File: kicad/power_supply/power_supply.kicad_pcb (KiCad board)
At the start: 2 copper layers, 4 parts

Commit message: Commit
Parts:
- added C1: 1u, Capacitor_SMD:C_0805_2012Metric_Pad1.18x1.45mm_HandSolder, F.Cu at (35.4, 41.0)
- added C14: 47u, Capacitor_SMD:C_0805_2012Metric_Pad1.18x1.45mm_HandSolder, F.Cu at (40.2, 47.0)
- added C15: 47u, Capacitor_SMD:C_0805_2012Metric_Pad1.18x1.45mm_HandSolder, F.Cu at (40.2, 50.0)
- added C16: 47u, Capacitor_SMD:C_0805_2012Metric_Pad1.18x1.45mm_HandSolder, F.Cu at (45.0, 41.0)
- added C17: 47u, Capacitor_SMD:C_0805_2012Metric_Pad1.18x1.45mm_HandSolder, F.Cu at (45.0, 44.0)
- added C18: 100n, Capacitor_SMD:C_0805_2012Metric_Pad1.18x1.45mm_HandSolder, F.Cu at (45.0, 47.0)
- added C19: 1u, Capacitor_SMD:C_0805_2012Metric_Pad1.18x1.45mm_HandSolder, F.Cu at (45.0, 50.0)
- added C7: 100n, Capacitor_SMD:C_0805_2012Metric_Pad1.18x1.45mm_HandSolder, F.Cu at (35.4, 50.0)
- added C8: 47u, Capacitor_SMD:C_0805_2012Metric_Pad1.18x1.45mm_HandSolder, F.Cu at (40.2, 41.0)
- added C9: 47u, Capacitor_SMD:C_0805_2012Metric_Pad1.18x1.45mm_HandSolder, F.Cu at (40.2, 44.0)
- added J2: USB_C_Receptacle_USB2.0, Connector_USB:USB_C_Receptacle_GCT_USB4085, F.Cu at (6.03, 57.0)
- added J6: Conn_02x08_Odd_Even, Connector_PinSocket_2.54mm:PinSocket_2x08_P2.54mm_Vertical, F.Cu at (60.0, 76.4)
- added JP1: Jumper_2_Open, Jumper:SolderJumper-2_P1.3mm_Open_Pad1.0x1.5mm, F.Cu at (2.35, 53.0)
- added Q7: NPN, Package_TO_SOT_THT:TO-220-3_Vertical, F.Cu at (50.6, 43.4)
- added Q8: PNP, Package_TO_SOT_THT:TO-220-3_Vertical, F.Cu at (50.6, 49.4)
- added R10: 22k, Resistor_SMD:R_0805_2012Metric_Pad1.20x1.40mm_HandSolder, F.Cu at (40.1, 38.0)
- added R11: 10k, Resistor_SMD:R_0805_2012Metric_Pad1.20x1.40mm_HandSolder, F.Cu at (44.8, 26.2)
- added R12: 10k, Resistor_SMD:R_0805_2012Metric_Pad1.20x1.40mm_HandSolder, F.Cu at (44.8, 29.2)
- added R15: 3k3, Resistor_SMD:R_0805_2012Metric_Pad1.20x1.40mm_HandSolder, F.Cu at (44.8, 32.1)
- added R16: 3k3, Resistor_SMD:R_0805_2012Metric_Pad1.20x1.40mm_HandSolder, F.Cu at (44.8, 35.1)
- added R17: 33k, Resistor_SMD:R_0805_2012Metric_Pad1.20x1.40mm_HandSolder, F.Cu at (44.8, 38.0)
- added R18: 1k, Resistor_SMD:R_0805_2012Metric_Pad1.20x1.40mm_HandSolder, F.Cu at (49.6, 26.2)
- added R19: 1k, Resistor_SMD:R_0805_2012Metric_Pad1.20x1.40mm_HandSolder, F.Cu at (49.6, 29.2)
- added R20: 33k, Resistor_SMD:R_0805_2012Metric_Pad1.20x1.40mm_HandSolder, F.Cu at (49.6, 32.1)
- added R23: 10k, Resistor_SMD:R_0805_2012Metric_Pad1.20x1.40mm_HandSolder, F.Cu at (49.6, 35.1)
- added R24: 16k, Resistor_SMD:R_0805_2012Metric_Pad1.20x1.40mm_HandSolder, F.Cu at (49.6, 38.0)
- added R3: 22, Resistor_SMD:R_0805_2012Metric_Pad1.20x1.40mm_HandSolder, F.Cu at (35.3, 32.1)
- added R4: 22, Resistor_SMD:R_0805_2012Metric_Pad1.20x1.40mm_HandSolder, F.Cu at (35.3, 35.1)
- added R5: 1k5, Resistor_SMD:R_0805_2012Metric_Pad1.20x1.40mm_HandSolder, F.Cu at (35.3, 38.0)
- added R6: 1M, Resistor_SMD:R_0805_2012Metric_Pad1.20x1.40mm_HandSolder, F.Cu at (40.1, 26.2)
- added R7: 22k, Resistor_SMD:R_0805_2012Metric_Pad1.20x1.40mm_HandSolder, F.Cu at (40.1, 29.2)
- added R8: 10k, Resistor_SMD:R_0805_2012Metric_Pad1.20x1.40mm_HandSolder, F.Cu at (40.1, 32.1)
- added R9: 10k, Resistor_SMD:R_0805_2012Metric_Pad1.20x1.40mm_HandSolder, F.Cu at (40.1, 35.1)
- added TH2: 20R->1R, Capacitor_THT:C_Disc_D9.0mm_W5.0mm_P5.00mm, F.Cu at (54.7, 28.0)
- added TH3: 20R->1R, Capacitor_THT:C_Disc_D9.0mm_W5.0mm_P5.00mm, F.Cu at (54.7, 34.6)
- added U1: PCM2707CPJTR, Package_QFP:TQFP-32_7x7mm_P0.8mm, F.Cu at (10.0, 72.0)
- added U2: LM317, Package_TO_SOT_SMD:SOT-89-3, F.Cu at (29.2, 50.2)
- C5: value 10u -> 100n
- R1: value 10k -> 5.1k
- R2: value 10k -> 1k5
- moved C5 23.7 mm to (35.4, 44.0)
- moved C6 23.5 mm to (35.4, 47.0)
- moved R1 16.6 mm to (35.3, 26.2)
- moved R2 16.1 mm to (35.3, 29.2)
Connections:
- C5 pad 1: +36V -> GNDD
- C5 pad 2: GND -> +3V3
- C6 pad 1: GND -> GNDD
- C6 pad 2: -36V -> Net-(U1-VCOM)
- R1 pad 1: +36V -> Net-(J2-CC1)
- R1 pad 2: GND -> GNDD
- R2 pad 1: GND -> Net-(D3-A2)
- R2 pad 2: -36V -> +3V3
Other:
- board outline added: 62 x 99 mm

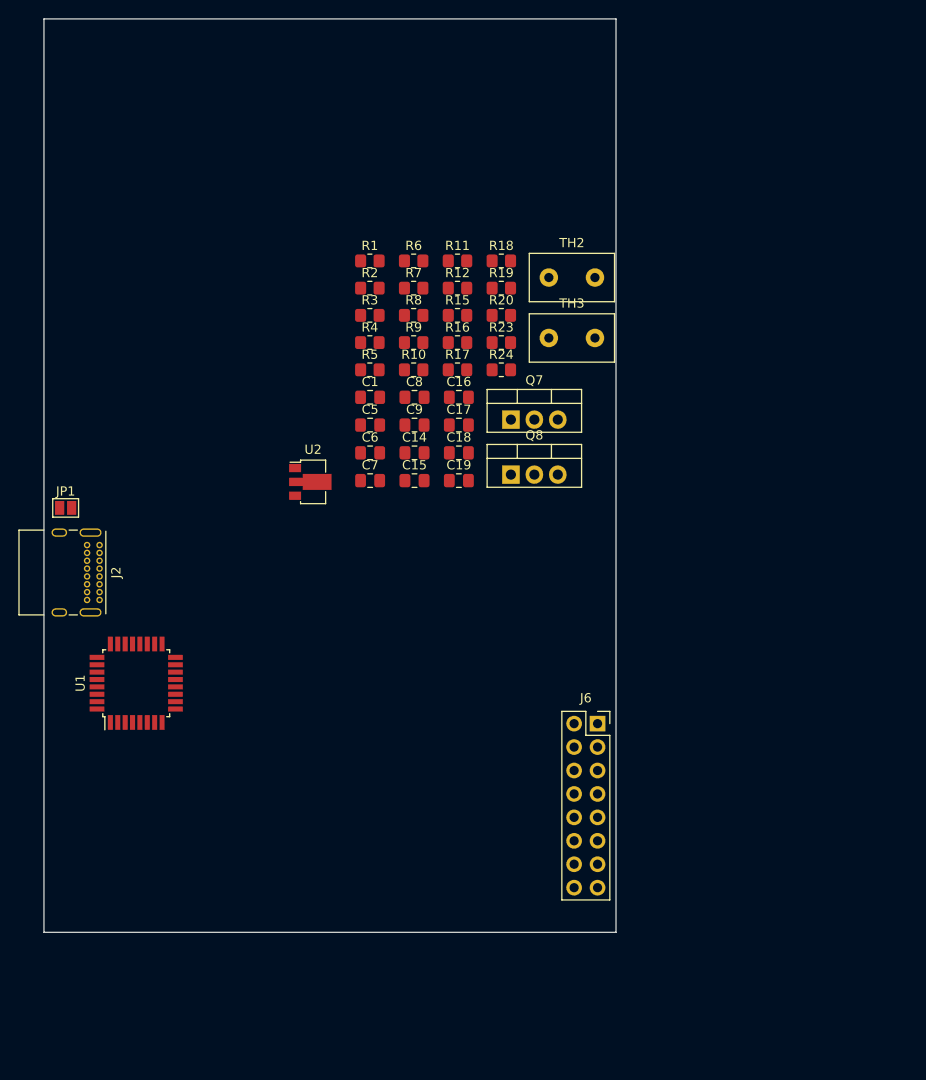
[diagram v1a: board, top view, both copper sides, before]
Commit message: completed power supply footprints and placement
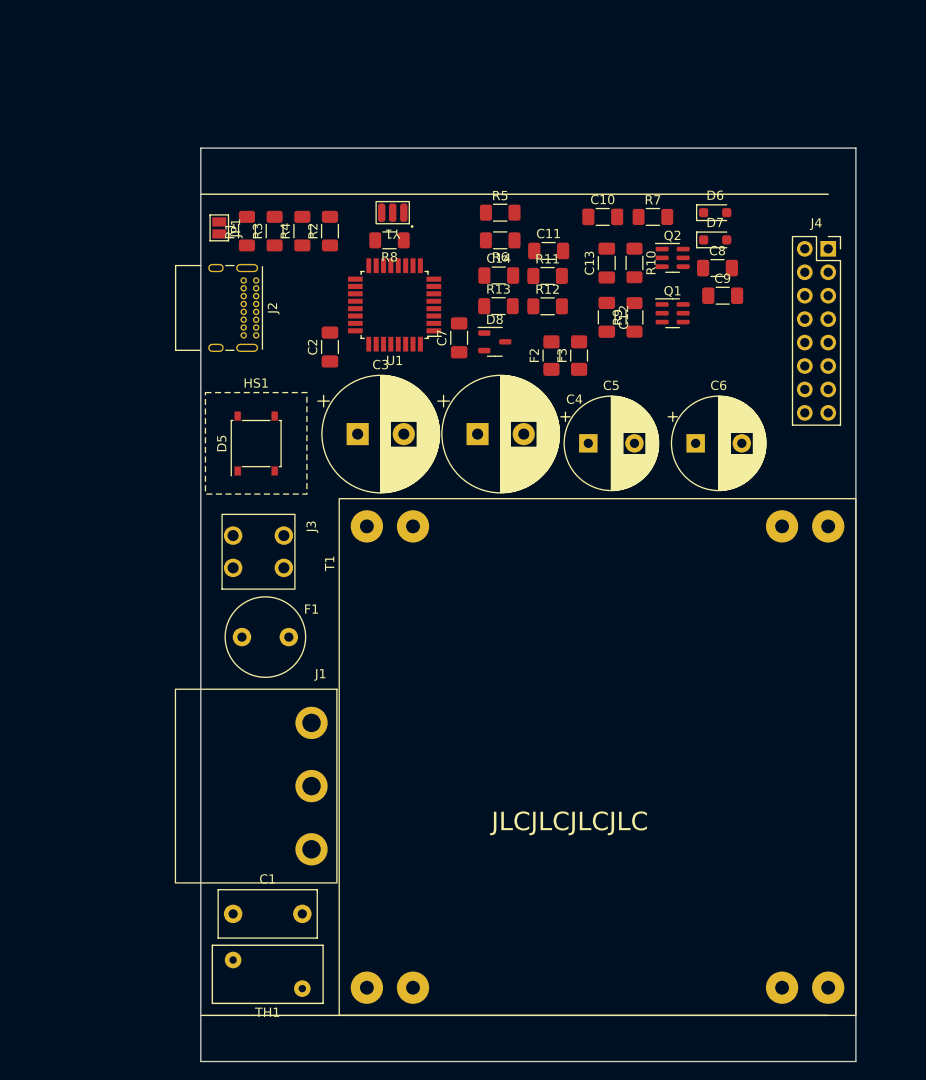
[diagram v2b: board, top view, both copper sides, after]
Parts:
- removed C15, C16, C17: 47u, Capacitor_SMD:C_0805_2012Metric_Pad1.18x1.45mm_HandSolder
- removed C18: 100n, Capacitor_SMD:C_0805_2012Metric_Pad1.18x1.45mm_HandSolder
- removed C19: 1u, Capacitor_SMD:C_0805_2012Metric_Pad1.18x1.45mm_HandSolder
- removed J6: Conn_02x08_Odd_Even, Connector_PinSocket_2.54mm:PinSocket_2x08_P2.54mm_Vertical
- removed Q7: NPN, Package_TO_SOT_THT:TO-220-3_Vertical
- removed Q8: PNP, Package_TO_SOT_THT:TO-220-3_Vertical
- removed R15, R16: 3k3, Resistor_SMD:R_0805_2012Metric_Pad1.20x1.40mm_HandSolder
- removed R17, R20: 33k, Resistor_SMD:R_0805_2012Metric_Pad1.20x1.40mm_HandSolder
- removed R18, R19: 1k, Resistor_SMD:R_0805_2012Metric_Pad1.20x1.40mm_HandSolder
- removed R23: 10k, Resistor_SMD:R_0805_2012Metric_Pad1.20x1.40mm_HandSolder
- removed R24: 16k, Resistor_SMD:R_0805_2012Metric_Pad1.20x1.40mm_HandSolder
- removed TH2, TH3: 20R->1R, Capacitor_THT:C_Disc_D9.0mm_W5.0mm_P5.00mm
- removed U2: LM317, Package_TO_SOT_SMD:SOT-89-3
- added C10: 10u, Capacitor_SMD:C_1206_3216Metric_Pad1.33x1.80mm_HandSolder, F.Cu at (60.6, 21.5)
- added C11: 100n, Capacitor_SMD:C_1206_3216Metric_Pad1.33x1.80mm_HandSolder, F.Cu at (54.7, 25.1)
- added C12: 10u, Capacitor_SMD:C_1206_3216Metric_Pad1.33x1.80mm_HandSolder, F.Cu at (61.0, 32.3)
- added C13: 10u, Capacitor_SMD:C_1206_3216Metric_Pad1.33x1.80mm_HandSolder, F.Cu at (61.0, 26.5)
- added C2: 1u, Capacitor_SMD:C_1206_3216Metric_Pad1.33x1.80mm_HandSolder, F.Cu at (31.0, 35.6)
- added C3: 2m2, Capacitor_THT:CP_Radial_D12.5mm_P5.00mm, F.Cu at (34.0, 45.0)
- added C4: 2m2, Capacitor_THT:CP_Radial_D12.5mm_P5.00mm, F.Cu at (47.0, 45.0)
- added D5: ~, Diode_SMD:Diode_Bridge_Vishay_MBLS, F.Cu at (23.0, 46.0)
- added D6: D, Diode_SMD:D_SOD-323_HandSoldering, F.Cu at (72.8, 21.0)
- added D7: D, Diode_SMD:D_SOD-323_HandSoldering, F.Cu at (72.8, 23.9)
- added D8: ~, Package_TO_SOT_SMD:SOT-23-3, F.Cu at (48.9, 35.0)
- added F1: 80mA, Fuse:Fuse_Littelfuse_372_D8.50mm, F.Cu at (26.5, 67.0)
- added F2: 1A, Fuse:Fuse_1206_3216Metric_Pad1.42x1.75mm_HandSolder, F.Cu at (55.0, 36.5)
- added F3: 1A, Fuse:Fuse_1206_3216Metric_Pad1.42x1.75mm_HandSolder, F.Cu at (58.0, 36.5)
- added HS1: Heatsink, library:Heatsink_10x10, F.Cu at (23.0, 46.0)
- added J1: Conn_WallSocket_Earth, library:WallSocket_Schurter_6160.0003, F.Cu at (29.0, 83.2)
- added J3: Conn_01x02, library:WAGO_2086-11X2, F.Cu at (23.2, 57.8)
- added J4: Conn_02x08_Odd_Even, Connector_PinSocket_2.54mm:PinSocket_2x08_P2.54mm_Vertical, F.Cu at (85.0, 24.9)
- added Q1: BCM53DS, Package_SO:SC-74-6_1.5x2.9mm_P0.95mm, F.Cu at (68.1, 31.9)
- added Q2: BCM56DS, Package_SO:SC-74-6_1.5x2.9mm_P0.95mm, F.Cu at (68.1, 25.9)
- added R13: 16, Resistor_SMD:R_1206_3216Metric_Pad1.30x1.75mm_HandSolder, F.Cu at (49.3, 31.1)
- added T1: 70043K, library:Talema_Transformer_2P2S_10VA, F.Cu at (60.0, 80.0)
- added TH1: MOV, Varistor:RV_Disc_D12mm_W6.3mm_P7.5mm, F.Cu at (20.5, 102.0)
- added Y1: 12MHz±0.05%, library:Resonator_Murata, F.Cu at (37.8, 21.0)
- C1: value 1u -> 3n9; footprint Capacitor_SMD:C_0805_2012Metric_Pad1.18x1.45mm_HandSolder -> Capacitor_THT:C_Disc_D10.5mm_W5.0mm_P7.50mm
- C14, C9: value 47u -> 100n; footprint Capacitor_SMD:C_0805_2012Metric_Pad1.18x1.45mm_HandSolder -> Capacitor_SMD:C_1206_3216Metric_Pad1.33x1.80mm_HandSolder
- C5: value 100n -> 470u; footprint Capacitor_SMD:C_0805_2012Metric_Pad1.18x1.45mm_HandSolder -> Capacitor_THT:CP_Radial_D10.0mm_P5.00mm
- C6: value 10u -> 470u; footprint Capacitor_SMD:C_0805_2012Metric_Pad1.18x1.45mm_HandSolder -> Capacitor_THT:CP_Radial_D10.0mm_P5.00mm
- C7: value 100n -> 10u; footprint Capacitor_SMD:C_0805_2012Metric_Pad1.18x1.45mm_HandSolder -> Capacitor_SMD:C_1206_3216Metric_Pad1.33x1.80mm_HandSolder
- C8: value 47u -> 10u; footprint Capacitor_SMD:C_0805_2012Metric_Pad1.18x1.45mm_HandSolder -> Capacitor_SMD:C_1206_3216Metric_Pad1.33x1.80mm_HandSolder
- R1, R11, R12, R2, R3, R4, R9: footprint Resistor_SMD:R_0805_2012Metric_Pad1.20x1.40mm_HandSolder -> Resistor_SMD:R_1206_3216Metric_Pad1.30x1.75mm_HandSolder
- R10: value 22k -> 10k; footprint Resistor_SMD:R_0805_2012Metric_Pad1.20x1.40mm_HandSolder -> Resistor_SMD:R_1206_3216Metric_Pad1.30x1.75mm_HandSolder
- R5: value 1k5 -> 10k; footprint Resistor_SMD:R_0805_2012Metric_Pad1.20x1.40mm_HandSolder -> Resistor_SMD:R_1206_3216Metric_Pad1.30x1.75mm_HandSolder
- R6: value 1M -> 10k; footprint Resistor_SMD:R_0805_2012Metric_Pad1.20x1.40mm_HandSolder -> Resistor_SMD:R_1206_3216Metric_Pad1.30x1.75mm_HandSolder
- R7: value 22k -> 1k5; footprint Resistor_SMD:R_0805_2012Metric_Pad1.20x1.40mm_HandSolder -> Resistor_SMD:R_1206_3216Metric_Pad1.30x1.75mm_HandSolder
- R8: value 10k -> 1M; footprint Resistor_SMD:R_0805_2012Metric_Pad1.20x1.40mm_HandSolder -> Resistor_SMD:R_1206_3216Metric_Pad1.30x1.75mm_HandSolder
- U1: value PCM2707CPJTR -> PCM2706CPJTR
- moved C1 57.9 mm to (20.5, 97.0)
- moved U1 49.6 mm to (38.0, 31.0), turned to 180 degrees
- moved C9 36.2 mm to (73.6, 30.0)
- moved C8 35.7 mm to (73.0, 27.0)
- moved C6 35.3 mm to (70.6, 46.0)
- moved JP1 34.6 mm to (19.0, 22.6), turned to -90 degrees
- moved J2 33.3 mm to (23.0, 28.4)
- moved R7 27.1 mm to (66.0, 21.5)
- moved R10 26.6 mm to (64.0, 26.4), turned to -90 degrees
- moved R9 24.1 mm to (64.0, 32.4), turned to 90 degrees
- moved C5 23.7 mm to (59.0, 46.0)
- moved R5 22.1 mm to (49.5, 21.0)
- moved C14 21.3 mm to (49.3, 27.8)
- moved C7 18.2 mm to (45.0, 34.6), turned to 90 degrees
- moved R4 14.1 mm to (28.0, 23.0), turned to 90 degrees
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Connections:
- net Net-(D2-A2) renamed /CONN_D-
- net Net-(D3-A2) renamed /CONN_D+
- net Net-(U1-D+) renamed /D+
- net Net-(U1-D-) renamed /D-
- C1 pad 1: GNDD -> Net-(J3-Pin_1)
- C1 pad 2: VBUS -> /NEUTRAL
- C14 pad 1: +30V -> GND
- C14 pad 2: GND -> Net-(D8-A)
- C5 pad 1: GNDD -> +25V
- C5 pad 2: +3V3 -> GND
- C6 pad 1: GNDD -> GND
- C6 pad 2: Net-(U1-VCOM) -> -25V
- C7 pad 1: GNDD -> Net-(C7-Pad1)
- C7 pad 2: Net-(U1-VCCP) -> GND
- C8 pad 1: Net-(Q1-G) -> GND
- C8 pad 2: GND -> Net-(C8-Pad2)
- C9 pad 1: GND -> GNDD
- C9 pad 2: Net-(Q2-G) -> +3V3
- R10 pad 1: Net-(Q2-G) -> Net-(C8-Pad2)
- R10 pad 2: Net-(D5--) -> -25V
- R11 pad 1: +30V -> Net-(C7-Pad1)
- R11 pad 2: GND -> /CM+
- R12 pad 1: GND -> Net-(C8-Pad2)
- R12 pad 2: -30V -> /CM-
- R5 pad 1: Net-(U1-DT) -> +25V
- R5 pad 2: +3V3 -> GND
- R6 pad 1: Net-(U1-XTI) -> GND
- R6 pad 2: Net-(U1-XTO) -> -25V
- R7 pad 1: Net-(D5-+) -> /DT
- R7 pad 2: Net-(Q1-G) -> +3V3
- R8 pad 1: Net-(Q1-G) -> /XTI
- R8 pad 2: GND -> /XTO
- R9 pad 1: GND -> +25V
- R9 pad 2: Net-(Q2-G) -> Net-(C7-Pad1)
- U1 pad 12: Net-(U1-XTI) -> /XTI
- U1 pad 13: Net-(U1-XTO) -> /XTO
- U1 pad 15: Net-(U1-DT) -> /DT
- U1 pad 16: GNDD -> +3V3
- U1 pad 3: VBUS -> GNDD
- U1 pad 32: Net-(U1-VCOM) -> /VCOM
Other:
- board size 62 x 99 mm -> 71 x 99 mm
- board text added: "1mm to panel PCB"
- board text added: "JLCJLCJLCJLC"

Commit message: commit
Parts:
- removed D6, D7: D, Diode_SMD:D_SOD-323_HandSoldering
- removed D8: ~, Package_TO_SOT_SMD:SOT-23-3
- removed J2: USB_C_Receptacle_USB2.0, Connector_USB:USB_C_Receptacle_GCT_USB4085
- removed Q1: BCM53DS, Package_SO:SC-74-6_1.5x2.9mm_P0.95mm
- removed Q2: BCM56DS, Package_SO:SC-74-6_1.5x2.9mm_P0.95mm
- added C15: 10u, Capacitor_SMD:C_1206_3216Metric_Pad1.33x1.80mm_HandSolder, F.Cu at (65.6, 25.8)
- added C16: 10u, Capacitor_SMD:C_1206_3216Metric_Pad1.33x1.80mm_HandSolder, F.Cu at (65.6, 29.1)
- added D1: ~, Package_TO_SOT_SMD:SOT-23-3, F.Cu at (26.9, 23.1)
- added D2: D_TVS_Quadruple, Package_TO_SOT_SMD:SOT-353_SC-70-5_Handsoldering, F.Cu at (65.3, 33.6)
- added D3: ~, Diode_SMD:Diode_Bridge_Vishay_MBLS, F.Cu at (24.0, 52.0)
- added D4: ~, Package_TO_SOT_SMD:SOT-23-3, F.Cu at (26.9, 27.6)
- added J5: Conn_02x08_Odd_Even, Connector_PinSocket_2.54mm:PinSocket_2x08_P2.54mm_Vertical, F.Cu at (91.0, 23.8)
- added R14: 1k1, Resistor_SMD:R_1206_3216Metric_Pad1.30x1.75mm_HandSolder, F.Cu at (83.5, 32.3)
- added R15: 100, Resistor_SMD:R_1206_3216Metric_Pad1.30x1.75mm_HandSolder, F.Cu at (83.5, 35.6)
- added U2: LM337_SOT223, Package_TO_SOT_SMD:SOT-223-3_TabPin2, F.Cu at (65.0, 41.0)
- added U3: PCM2706CPJTR, Package_QFP:TQFP-32_7x7mm_P0.8mm, F.Cu at (45.0, 26.0)
- C1: value 3n9 -> 100n; footprint Capacitor_THT:C_Disc_D10.5mm_W5.0mm_P7.50mm -> Capacitor_SMD:C_1206_3216Metric_Pad1.33x1.80mm_HandSolder
- C10, C13, C8: value 10u -> 100n
- C11, C9: value 100n -> 10u
- C2: value 1u -> 4n7
- C3: value 2m2 -> 3n9; footprint Capacitor_THT:CP_Radial_D12.5mm_P5.00mm -> Capacitor_THT:C_Disc_D10.5mm_W5.0mm_P7.50mm
- C4: value 2m2 -> 100n; footprint Capacitor_THT:CP_Radial_D12.5mm_P5.00mm -> Capacitor_SMD:C_1206_3216Metric_Pad1.33x1.80mm_HandSolder
- C5: value 470u -> 3u3; footprint Capacitor_THT:CP_Radial_D10.0mm_P5.00mm -> Capacitor_SMD:C_1206_3216Metric_Pad1.33x1.80mm_HandSolder
- C7: value 10u -> 470u; footprint Capacitor_SMD:C_1206_3216Metric_Pad1.33x1.80mm_HandSolder -> Capacitor_THT:CP_Radial_D10.0mm_P5.00mm
- D5: footprint Diode_SMD:Diode_Bridge_Vishay_MBLS -> Package_TO_SOT_SMD:SOT-23-3
- F2, F3: value 1A -> 500mA; footprint Fuse:Fuse_1206_3216Metric_Pad1.42x1.75mm_HandSolder -> Fuse:Fuse_Schurter_UMT250; moved to B.Cu
- J3: value Conn_01x02 -> USB_C_Receptacle_USB2.0; footprint library:WAGO_2086-11X2 -> Connector_USB:USB_C_Receptacle_GCT_USB4085
- J4: value Conn_02x08_Odd_Even -> Conn_01x02; footprint Connector_PinSocket_2.54mm:PinSocket_2x08_P2.54mm_Vertical -> library:WAGO_2086-11X2
- R1: value 5.1k -> 22
- R11: value 10k -> 1M
- R12: value 10k -> 100
- R13: value 16 -> 1k1
- R2: value 1k5 -> 33k
- R3, R4: value 22 -> 5k1
- R5: value 10k -> 1k5
- R6: value 10k -> 22
- R7: value 1k5 -> 22
- R8: value 1M -> 1k5
- T1: value 70043K -> 70063K; footprint library:Talema_Transformer_2P2S_10VA -> library:Talema_Transformer_2P2S_25VA
- U1: value PCM2706CPJTR -> LM317_SOT-223; footprint Package_QFP:TQFP-32_7x7mm_P0.8mm -> Package_TO_SOT_SMD:SOT-223-3_TabPin2
- moved C1 81.6 mm to (53.6, 22.4)
- moved J4 64.5 mm to (22.8, 41.8), turned to 90 degrees
- moved C3 53.5 mm to (21.2, 97.0)
- moved R1 49.6 mm to (71.6, 22.4), turned to 0 degrees
- moved R3 47.0 mm to (71.6, 29.0), turned to 0 degrees
- moved R4 44.6 mm to (71.6, 32.3), turned to 0 degrees
- moved R2 40.7 mm to (71.6, 25.7), turned to 0 degrees
- moved R8 40.4 mm to (77.5, 29.0), turned to 0 degrees
- moved C6 39.3 mm to (32.0, 39.0)
- moved R13 34.3 mm to (83.5, 29.0)
- moved J3 29.6 mm to (22.6, 28.2), turned to -90 degrees
- moved R11 29.4 mm to (83.5, 22.4)
- moved R12 29.4 mm to (83.5, 25.7)
- moved R6 28.1 mm to (77.5, 22.4), turned to 0 degrees
- moved R5 26.5 mm to (71.6, 35.6)
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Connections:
- C1 pad 1: Net-(J3-Pin_1) -> GND
- C1 pad 2: /NEUTRAL -> Net-(J1-EARTH)
- C10 pad 2: /VCOM -> Net-(U3-VCCP)
- C11 pad 1: GNDD -> Net-(D4-A)
- C11 pad 2: Net-(U1-VCCP) -> GND
- C12 pad 1: /CM+ -> GND
- C12 pad 2: GND -> Net-(D5-K)
- C13 pad 1: GND -> +20Vreg
- C13 pad 2: /CM- -> GND
- C14 pad 2: Net-(D8-A) -> -20Vreg
- C2 pad 1: GNDD -> Net-(D2-C)
- C2 pad 2: VBUS -> GNDD
- C3 pad 1: +25V -> Net-(J4-Pin_1)
- C3 pad 2: GND -> /NEUTRAL
- C4 pad 1: GND -> GNDD
- C4 pad 2: -25V -> VBUS
- C5 pad 1: +25V -> GNDD
- C5 pad 2: GND -> VBUS
- C6 pad 1: GND -> +25V
- C6 pad 2: -25V -> GND
- C7 pad 1: Net-(C7-Pad1) -> GND
- C7 pad 2: GND -> -25V
- C8 pad 1: GND -> GNDD
- C8 pad 2: Net-(C8-Pad2) -> +3V3
- C9 pad 2: +3V3 -> /VCOM
- D5 pad 1: /V_{rect}+ -> -25V
- D5 pad 2: /V_{tran}- -> -20Vreg
- D5 pad 3: /V_{rect}- -> Net-(D5-K)
- F1 pad 2: Net-(J3-Pin_1) -> Net-(J4-Pin_1)
- J1 pad 3: Net-(D8-A) -> Net-(J1-EARTH)
- J4 pad 1: +20Vreg -> Net-(J4-Pin_1)
- J4 pad 2: +25V -> /LIVE
- JP1 pad 2: Net-(J2-SHIELD) -> Net-(D2-C)
- R1 pad 1: Net-(J2-CC1) -> Net-(J1-EARTH)
- R1 pad 2: GNDD -> GND
- R10 pad 1: Net-(C8-Pad2) -> GND
- R11 pad 1: Net-(C7-Pad1) -> /XTI
- R11 pad 2: /CM+ -> /XTO
- R12 pad 1: Net-(C8-Pad2) -> +20Vreg
- R12 pad 2: /CM- -> Net-(D4-A)
- R13 pad 1: Net-(D8-A) -> Net-(D4-A)
- R2 pad 1: /CONN_D+ -> GNDD
- R2 pad 2: +3V3 -> Net-(D2-C)
- R3 pad 1: /CONN_D- -> Net-(J3-CC1)
- R3 pad 2: /D- -> GNDD
- R4 pad 1: /CONN_D+ -> Net-(J3-CC2)
- R4 pad 2: /D+ -> GNDD
- R5 pad 1: +25V -> /CONN_D+
- R5 pad 2: GND -> +3V3
- R6 pad 1: GND -> /CONN_D-
- R6 pad 2: -25V -> /D-
- R7 pad 1: /DT -> /CONN_D+
- R7 pad 2: +3V3 -> /D+
- R8 pad 1: /XTI -> /DT
- R8 pad 2: /XTO -> +3V3
- R9 pad 2: Net-(C7-Pad1) -> GND
- TH1 pad 1: Net-(J3-Pin_1) -> Net-(J4-Pin_1)
- U1 pad 1: GNDD -> Net-(D4-A)
- U1 pad 2: Net-(U1-VCCP) -> +20Vreg
- U1 pad 3: GNDD -> +25V
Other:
- board size 71 x 99 mm -> 76.5 x 99 mm
- board text added: "front face of front plate"
- board text removed: "1mm to panel PCB"
- board text removed: "JLCJLCJLCJLC"
